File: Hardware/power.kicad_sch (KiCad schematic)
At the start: 13 parts, among them U3 LM285D-2.5, U4 AMS1117-3.3

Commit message: Version 0.1
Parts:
- removed FB1: FerriteBead, Resistor_SMD:R_0805_2012Metric_Pad1.20x1.40mm_HandSolder, symbol Device:FerriteBead
- removed TP0: Test_GND, TestPoint:TestPoint_Pad_D1.5mm, symbol Connector:TestPoint
- removed TP1: Test_5V, TestPoint:TestPoint_Pad_D1.5mm, symbol Connector:TestPoint
- removed U4: AMS1117-3.3, Package_TO_SOT_SMD:SOT-223-3_TabPin2, symbol Regulator_Linear:AMS1117-3.3
- added C19: 10uF, symbol Device:C
- added C20: 0.1uF, symbol Device:C
- added D2: POWER LED, LED_SMD:LED_0805_2012Metric_Pad1.15x1.40mm_HandSolder, symbol Device:LED
- added J1: I2C Debug, Connector_JST:JST_XH_B4B-XH-A_1x04_P2.50mm_Vertical, symbol Connector_Generic:Conn_01x04
- added J2: I2C, Connector_JST:JST_SH_SM04B-SRSS-TB_1x04-1MP_P1.00mm_Horizontal, symbol Connector_Generic:Conn_01x04
- added L1: INDUCTOR, Inductor_SMD:L_0603_1608Metric, symbol pspice:INDUCTOR
- added R11, R12: 10k, symbol Device:R
- added R16: 150, Resistor_SMD:R_0603_1608Metric_Pad0.98x0.95mm_HandSolder, symbol Device:R
- added R17: 316k, Resistor_SMD:R_0603_1608Metric_Pad0.98x0.95mm_HandSolder, symbol Device:R
- added R18: 100k, Resistor_SMD:R_0603_1608Metric_Pad0.98x0.95mm_HandSolder, symbol Device:R
- added U4: TPS61023DRLR, TPS61023DRLR:Texas_Instruments_-_TPS61023DRLR, symbol Texas_Instruments_-_TPS61023DRLR:TPS61023DRLR
- added U7: AP7312-1833W6-7, symbol AP7312-1833W6-7:AP7312-1833W6-7
- C11: value 10u -> 2.2uF; footprint Capacitor_SMD:C_0805_2012Metric_Pad1.18x1.45mm_HandSolder -> Capacitor_SMD:C_0603_1608Metric_Pad1.08x0.95mm_HandSolder
- C12: value 22u -> 2.2uF; footprint Capacitor_SMD:C_0805_2012Metric_Pad1.18x1.45mm_HandSolder -> Capacitor_SMD:C_0603_1608Metric_Pad1.08x0.95mm_HandSolder
- C13, C16, C17: footprint Capacitor_SMD:C_0805_2012Metric_Pad1.18x1.45mm_HandSolder -> Capacitor_SMD:C_0603_1608Metric_Pad1.08x0.95mm_HandSolder
- C14: value 100n -> 10uF; footprint Capacitor_SMD:C_0805_2012Metric_Pad1.18x1.45mm_HandSolder -> (none)
- C15: value 10 -> 10uF; footprint Capacitor_SMD:C_0805_2012Metric_Pad1.18x1.45mm_HandSolder -> (none)
- R20: footprint Resistor_SMD:R_0805_2012Metric_Pad1.20x1.40mm_HandSolder -> Resistor_SMD:R_0603_1608Metric_Pad0.98x0.95mm_HandSolder
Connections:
- net +3V3: now also C11.1, C14.2, C15.2, J1.2 (Pin_2), J2.2 (Pin_2), L1.1, R11.1, R12.2, R16.1, U4.3 (VIN), U7.1 (OUT2), U7.5 (IN)
- net GND: now also C14.1, C15.1, C19.1, C20.1, D2.1 (K), J1.1 (Pin_1), J2.1 (Pin_1), R18.2, U4.2 (EN), U4.4 (GND), U7.2 (GND); no longer C14.2, C15.2
- net +5V: no longer names the net of C12.1, R20.1
- net +5V: now also R17.1, U4.6 (VOUT); no longer C14.1
- removed net +5VD: C11.1, C15.1
- new net: R17.2, R18.1, U4.1 (FB)
- new net: D2.2 (A), R16.2
- new net: L1.2, U4.5 (SW)
- new net: U7.3 (EN2), U7.4 (EN1)
- new net +1V8: C19.2, C20.2, U7.6 (OUT1)
- new net SCL: J1.4 (Pin_4), J2.4 (Pin_4), R11.2
- new net SDA: J1.3 (Pin_3), J2.3 (Pin_3), R12.1
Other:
- note added: "1.8V for Color sensor"
- note added: "Connectors"
- note added: "I2C Pullup & Shift"
- note added: "Main Power Supply +3.3v"
- note removed: "Main Power Supply +5V"
- moved on the sheet: C13, C16, C17, R20, U3

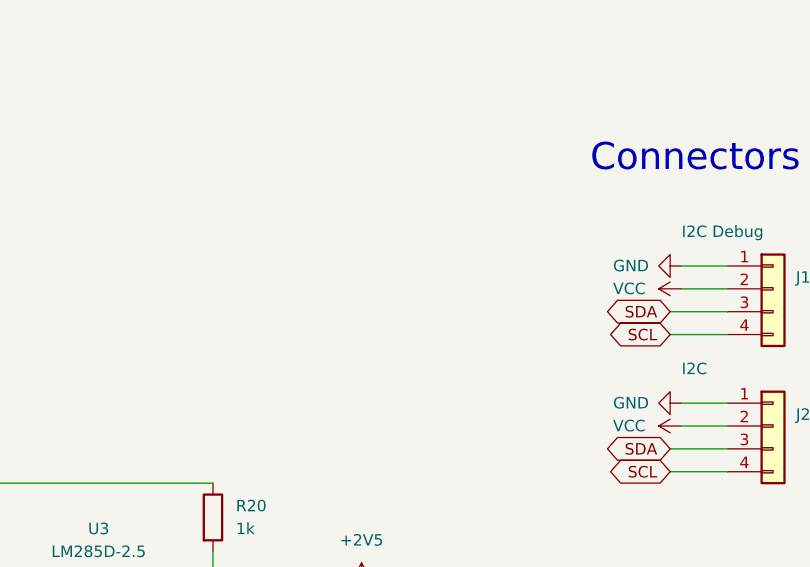
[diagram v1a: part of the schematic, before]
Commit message: Readme + hole update
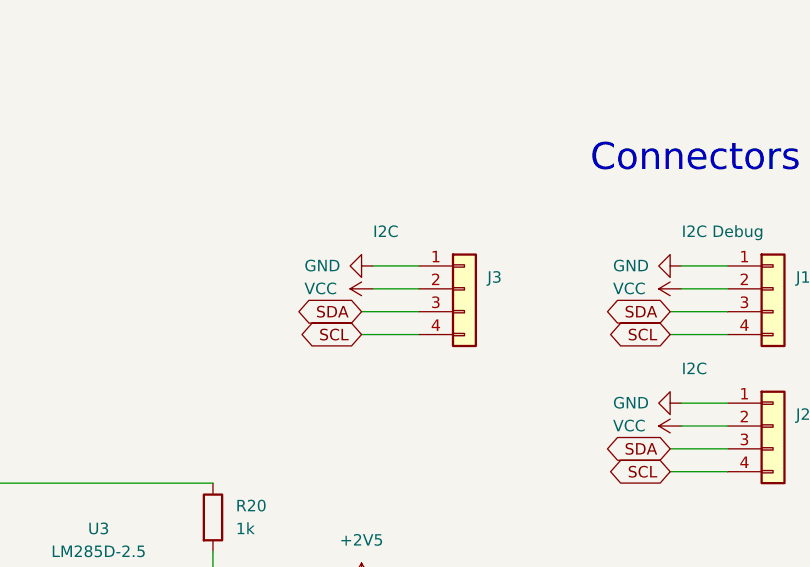
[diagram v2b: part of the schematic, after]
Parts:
- added J3: I2C, Connector_JST:JST_SH_SM04B-SRSS-TB_1x04-1MP_P1.00mm_Horizontal, symbol Connector_Generic:Conn_01x04
- C14, C15, C19, C20: footprint (none) -> Capacitor_SMD:C_0603_1608Metric_Pad1.08x0.95mm_HandSolder
- R11, R12: footprint (none) -> Resistor_SMD:R_0603_1608Metric_Pad0.98x0.95mm_HandSolder
- U7: footprint (none) -> AP7312-1833W6-7:AP7312-1833W6-7
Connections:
- net +3V3: now also J3.2 (Pin_2)
- net GND: now also J3.1 (Pin_1)
- net SCL: now also J3.4 (Pin_4)
- net SDA: now also J3.3 (Pin_3)
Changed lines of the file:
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@@
+    (stroke (width 0) (type default) (color 0 0 0 0))
+  )
+  (wire (pts (xy 151.13 142.24) (xy 157.48 142.24))
     (stroke (width 0) (type default) (color 0 0 0 0))
   )
@@
     (stroke (width 0) (type default) (color 0 0 0 0))
   )
+  (wire (pts (xy 152.4 137.16) (xy 157.48 137.16))
+    (stroke (width 0) (type default) (color 0 0 0 0))
+  )
   (wire (pts (xy 34.29 171.45) (xy 34.29 185.42))
     (stroke (width 0) (type default) (color 0 0 0 0))
@@
     (stroke (width 0) (type default) (color 0 0 0 0))
   )
+  (wire (pts (xy 151.13 144.78) (xy 157.48 144.78))
+    (stroke (width 0) (type default) (color 0 0 0 0))
+  )
   (wire (pts (xy 134.62 168.91) (xy 134.62 172.72))
     (stroke (width 0) (type default) (color 0 0 0 0))
@@
   )
   (wire (pts (xy 83.82 185.42) (xy 92.71 185.42))
+    (stroke (width 0) (type default) (color 0 0 0 0))
+  )
+  (wire (pts (xy 152.4 139.7) (xy 157.48 139.7))
     (stroke (width 0) (type default) (color 0 0 0 0))
   )
@@
     )
   )
+  (global_label "SDA" (shape bidirectional) (at 151.13 142.24 180) (fields_autoplaced)
+    (effects (font (size 1.27 1.27)) (justify right))
+    (property "Intersheet References" "${INTERSHEET_REFS}" (id 0) (at 145.1488 142.3194 0)
+      (effects (font (size 1.27 1.27)) (justify right) hide)
+    )
+  )
   (global_label "SCL" (shape bidirectional) (at 181.61 46.99 180) (fields_autoplaced)
     (effects (font (size 1.27 1.27)) (justify right))
@@
     )
   )
+  (global_label "SCL" (shape bidirectional) (at 151.13 144.78 180) (fields_autoplaced)
+    (effects (font (size 1.27 1.27)) (justify right))
+    (property "Intersheet References" "${INTERSHEET_REFS}" (id 0) (at 145.2093 144.7006 0)
+      (effects (font (size 1.27 1.27)) (justify right) hide)
+    )
+  )
+  (symbol (lib_id "power:VCC") (at 152.4 139.7 90) (unit 1)
+    (in_bom yes) (on_board yes)
+    (property "Reference" "#PWR05" (id 0) (at 156.21 139.7 0)
+      (effects (font (size 1.27 1.27)) hide)
+    )
+    (property "Value" "VCC" (id 1) (at 144.78 139.7 90)
+      (effects (font (size 1.27 1.27)) (justify right))
+    )
+    (property "Footprint" "" (id 2) (at 152.4 139.7 0)
+      (effects (font (size 1.27 1.27)) hide)
+    )
+    (property "Datasheet" "" (id 3) (at 152.4 139.7 0)
+      (effects (font (size 1.27 1.27)) hide)
+    )
+    (pin "1")
+  )
   (symbol (lib_id "Device:C") (at 58.42 83.82 0) (unit 1)
     (in_bom yes) (on_board yes) (fields_autoplaced)
@@
     (property "Reference" "R12" (id 0) (at 189.23 49.53 90))
     (property "Value" "10k" (id 1) (at 189.23 52.07 90))
-    (property "Footprint" "" (id 2) (at 189.23 53.848 90)
+    (property "Footprint" "Resistor_SMD:R_0603_1608Metric_Pad0.98x0.95mm_HandSolder" (id 2) (at 189.23 53.848 90)
       (effects (font (size 1.27 1.27)) hide)
     )
@@
     (pin "2")
   )
+  (symbol (lib_id "Connector_Generic:Conn_01x04") (at 162.56 139.7 0) (unit 1)
+    (in_bom yes) (on_board yes)
+    (property "Reference" "J3" (id 0) (at 165.1 138.4299 0)
+      (effects (font (size 1.27 1.27)) (justify left))
+    )
+    (property "Value" "I2C" (id 1) (at 152.4 133.35 0)
+      (effects (font (size 1.27 1.27)) (justify left))
+    )
+    (property "Footprint" "Connector_JST:JST_SH_SM04B-SRSS-TB_1x04-1MP_P1.00mm_Horizontal" (id 2) (at 162.56 139.7 0)
+      (effects (font (size 1.27 1.27)) hide)
+    )
+    (property "Datasheet" "~" (id 3) (at 162.56 139.7 0)
+      (effects (font (size 1.27 1.27)) hide)
+    )
+    (pin "1")
+    (pin "2")
+    (pin "3")
+    (pin "4")
+  )
   (symbol (lib_id "power:+1V8") (at 260.35 85.09 0) (unit 1)
     (in_bom yes) (on_board yes) (fields_autoplaced)
@@
       (effects (font (size 1.27 1.27)) (justify left))
     )
-    (property "Footprint" "" (id 2) (at 249.2248 96.52 0)
+    (property "Footprint" "Capacitor_SMD:C_0603_1608Metric_Pad1.08x0.95mm_HandSolder" (id 2) (at 249.2248 96.52 0)
       (effects (font (size 1.27 1.27)) hide)
     )
@@
       (effects (font (size 1.27 1.27)) (justify left))
     )
-    (property "Footprint" "" (id 2) (at 259.3848 96.52 0)
+    (property "Footprint" "Capacitor_SMD:C_0603_1608Metric_Pad1.08x0.95mm_HandSolder" (id 2) (at 259.3848 96.52 0)
       (effects (font (size 1.27 1.27)) hide)
     )
@@
     (property "Reference" "R11" (id 0) (at 189.23 44.45 90))
     (property "Value" "10k" (id 1) (at 189.23 46.99 90))
-    (property "Footprint" "" (id 2) (at 189.23 45.212 90)
+    (property "Footprint" "Resistor_SMD:R_0603_1608Metric_Pad0.98x0.95mm_HandSolder" (id 2) (at 189.23 45.212 90)
       (effects (font (size 1.27 1.27)) hide)
     )
@@
       (effects (font (size 1.27 1.27)) (justify left))
     )
-    (property "Footprint" "" (id 2) (at 159.0548 90.17 0)
+    (property "Footprint" "Capacitor_SMD:C_0603_1608Metric_Pad1.08x0.95mm_HandSolder" (id 2) (at 159.0548 90.17 0)
       (effects (font (size 1.27 1.27)) hide)
     )
@@
     (pin "1")
   )
+  (symbol (lib_id "power:GND") (at 152.4 137.16 270) (unit 1)
+    (in_bom yes) (on_board yes)
+    (property "Reference" "#PWR03" (id 0) (at 146.05 137.16 0)
+      (effects (font (size 1.27 1.27)) hide)
+    )
+    (property "Value" "GND" (id 1) (at 144.78 137.16 90)
+      (effects (font (size 1.27 1.27)) (justify left))
+    )
+    (property "Footprint" "" (id 2) (at 152.4 137.16 0)
+      (effects (font (size 1.27 1.27)) hide)
+    )
+    (property "Datasheet" "" (id 3) (at 152.4 137.16 0)
+      (effects (font (size 1.27 1.27)) hide)
+    )
+    (pin "1")
+  )
   (symbol (lib_id "Device:C") (at 270.51 100.33 180) (unit 1)
     (in_bom yes) (on_board yes)
@@
       (effects (font (size 1.27 1.27)) (justify left))
     )
-    (property "Footprint" "" (id 2) (at 269.5448 96.52 0)
+    (property "Footprint" "Capacitor_SMD:C_0603_1608Metric_Pad1.08x0.95mm_HandSolder" (id 2) (at 269.5448 96.52 0)
       (effects (font (size 1.27 1.27)) hide)
     )
@@
       (effects (font (size 1.524 1.524)))
     )
-    (property "Footprint" "" (id 2) (at 207.01 84.074 0)
+    (property "Footprint" "AP7312-1833W6-7:AP7312-1833W6-7" (id 2) (at 207.01 84.074 0)
       (effects (font (size 1.524 1.524)) hide)
     )

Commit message: Added hole placement measurements
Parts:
- J1: footprint Connector_JST:JST_XH_B4B-XH-A_1x04_P2.50mm_Vertical -> (none)
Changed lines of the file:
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@@
       (effects (font (size 1.27 1.27)) (justify left))
     )
-    (property "Footprint" "Connector_JST:JST_XH_B4B-XH-A_1x04_P2.50mm_Vertical" (id 2) (at 196.85 139.7 0)
+    (property "Footprint" "" (id 2) (at 196.85 139.7 0)
       (effects (font (size 1.27 1.27)) hide)
     )

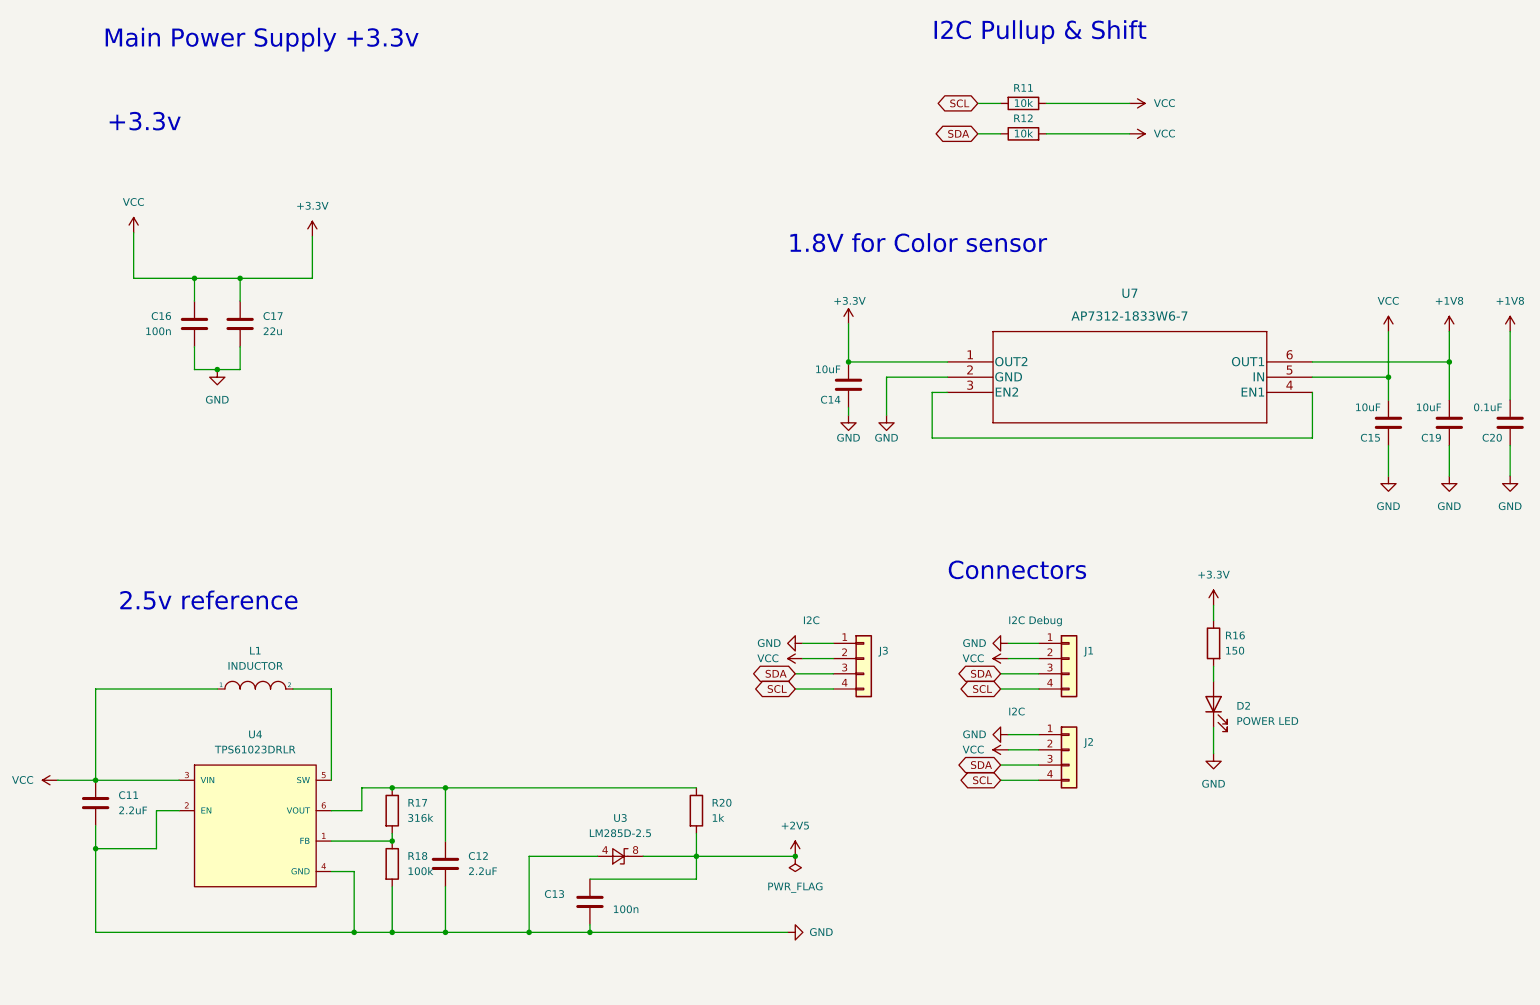
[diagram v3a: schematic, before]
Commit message: removed TP561023, added footprint libraries
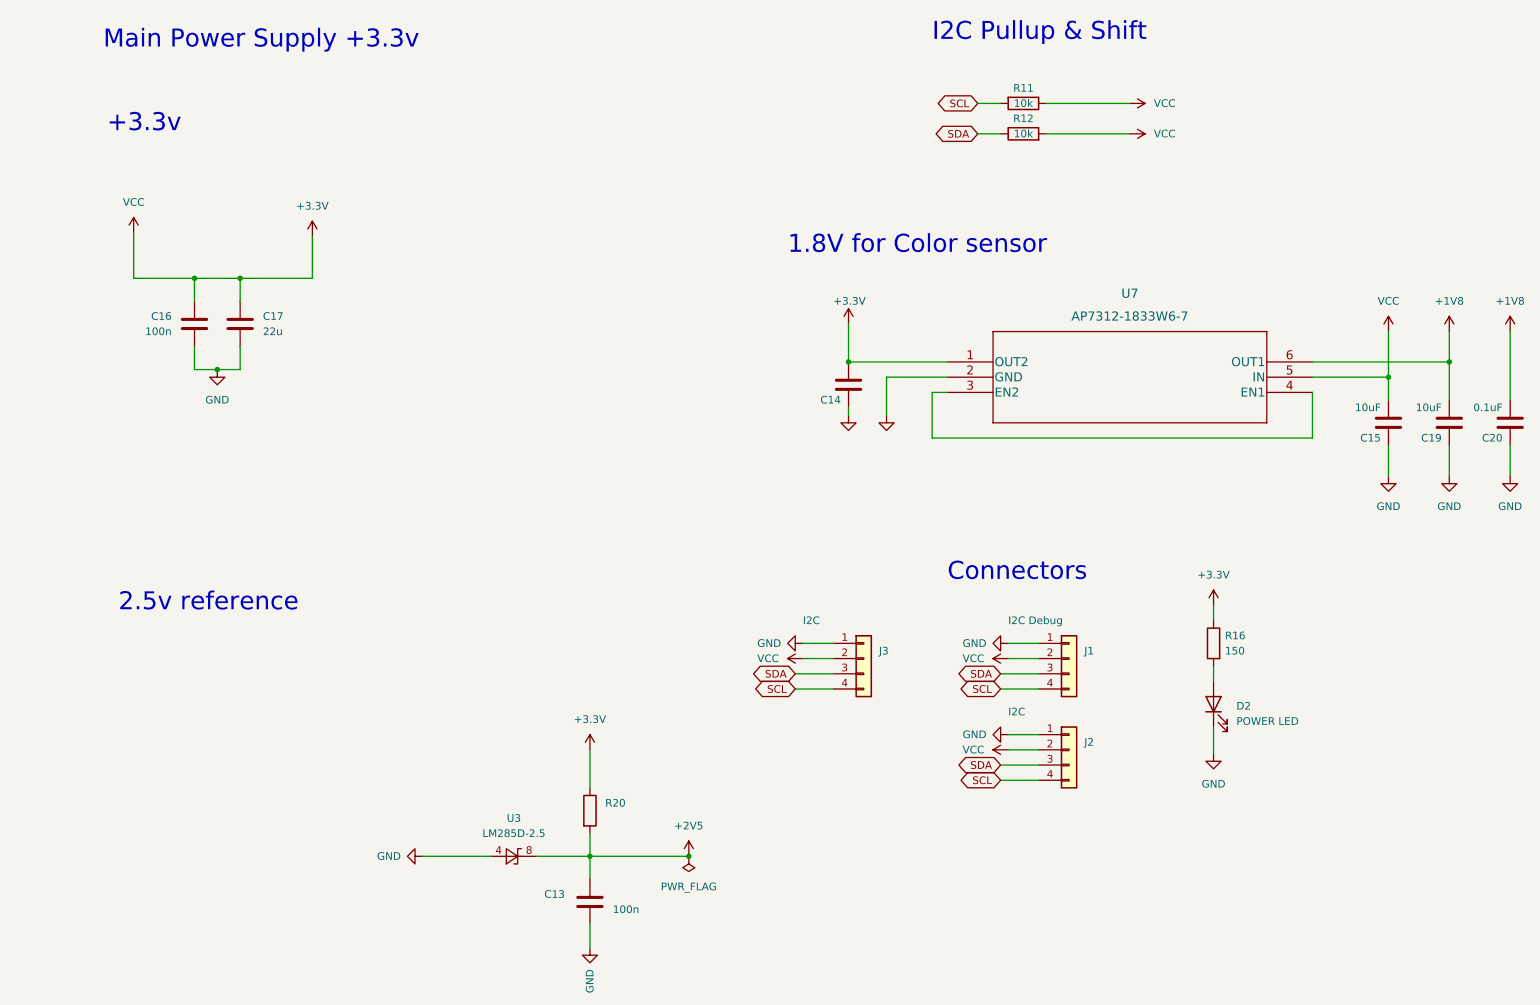
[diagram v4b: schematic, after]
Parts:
- removed C11, C12: 2.2uF, Capacitor_SMD:C_0603_1608Metric_Pad1.08x0.95mm_HandSolder, symbol Device:C
- removed L1: INDUCTOR, Inductor_SMD:L_0603_1608Metric, symbol pspice:INDUCTOR
- removed R17: 316k, Resistor_SMD:R_0603_1608Metric_Pad0.98x0.95mm_HandSolder, symbol Device:R
- removed R18: 100k, Resistor_SMD:R_0603_1608Metric_Pad0.98x0.95mm_HandSolder, symbol Device:R
- removed U4: TPS61023DRLR, TPS61023DRLR:Texas_Instruments_-_TPS61023DRLR, symbol Texas_Instruments_-_TPS61023DRLR:TPS61023DRLR
- C14: value 10uF -> (none); footprint Capacitor_SMD:C_0603_1608Metric_Pad1.08x0.95mm_HandSolder -> (none)
- J1: footprint (none) -> Connector_PinHeader_2.54mm:PinHeader_1x04_P2.54mm_Vertical
- R20: value 1k -> (none)
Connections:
- net +3V3: now also R20.1
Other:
- moved on the sheet: R20, U3

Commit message: Updated power design
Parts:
- C14: value (none) -> 10uF; footprint (none) -> Capacitor_SMD:C_0603_1608Metric_Pad1.08x0.95mm_HandSolder
- R20: value (none) -> 435
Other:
- moved on the sheet: C13, R20, U3
